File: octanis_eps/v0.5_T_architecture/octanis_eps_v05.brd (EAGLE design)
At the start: 100 x 80 mm, 141 parts, among them IC1 OPA2333DGK, Q3 32.768kHz, Q4 BSS123, U1 BQ24650_RVA_16, U10 CSD16327Q3_DQG_8, U13 CSD16327Q3_DQG_8, U14 CSD16327Q3_DQG_8, U2 TPS630250, U3 TPS630250, U4 TPS630250, U5 TPS2022D, U6 TPS61232, U7 CSD16327Q3_DQG_8, U8 MSP430G2544, U9 CSD16327Q3_DQG_8

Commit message: Arranged parts for EPS v05
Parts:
- moved JP6 220.5 mm to (76.2, 25.4), turned to 90 degrees
- moved JP3 204.9 mm to (11.4, 47.0)
- moved U14 191.1 mm to (72.4, 43.2), turned to 90 degrees
- moved R41 185.6 mm to (2.54, 41.9), turned to 270 degrees
- moved JP1 185.5 mm to (2.54, 47.0), turned to 90 degrees
- moved JP5 185.1 mm to (38.1, 5.08), turned to 90 degrees
- moved R14 184.1 mm to (73.7, 39.4), turned to 270 degrees
- moved R15 180.9 mm to (71.1, 39.4), turned to 90 degrees
- moved JP2 180.1 mm to (15.2, 29.2)
- moved U10 179.8 mm to (67.3, 43.2), turned to 90 degrees
- moved JP4 175.4 mm to (2.54, 6.35), turned to 90 degrees
- moved R10 172.7 mm to (68.6, 39.4), turned to 270 degrees
- moved R11 169.6 mm to (66.0, 39.4), turned to 90 degrees
- moved U13 168.4 mm to (62.2, 43.2), turned to 90 degrees
- moved R34 168.0 mm to (6.35, 5.08), flipped to the bottom, turned to 180 degrees
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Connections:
- removed net N$79: 6.8UH.2, R_SENSE2.I2
- new net N$4: 6.8UH.2, R_SENSE2.I1
- net BAT_OUT: now also JP6.11, JP6.13, JP6.15; no longer JP6.12, JP6.14, JP6.16
- net HEAT1: now also JP6.12; no longer JP6.11
- net HEAT2: now also JP6.14; no longer JP6.13
- net HEAT3: now also JP6.16; no longer JP6.15
- net N$77: now also R_SENSE2.V1; no longer R_SENSE2.V2
- net N$78: now also R_SENSE2.V2; no longer R_SENSE2.V1
- net SC_OUT: now also R_SENSE2.I2; no longer R_SENSE2.I1
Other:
- board size 100 x 80 mm -> 80 x 50 mm

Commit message: started manual routing
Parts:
- moved C15 11.1 mm to (28.1, 44.1), turned to 90 degrees
- moved C16 11.1 mm to (39.8, 42.3), turned to 90 degrees
- moved R116 9.55 mm to (37.1, 33.9), turned to 270 degrees
- moved R118 9.52 mm to (33.9, 32.6), turned to 180 degrees
- moved R103 8.86 mm to (27.6, 36.8), turned to 180 degrees
- moved R17 8.78 mm to (30.1, 44.1), turned to 270 degrees
- moved R13 8.56 mm to (37.7, 42.3), turned to 270 degrees
- moved R107 8.38 mm to (27.6, 39.4), turned to 180 degrees
- moved R119 6.13 mm to (37.7, 38.1), turned to 270 degrees
- moved R117 6.11 mm to (33.9, 34.9), turned to 0 degrees
- moved R104 5.55 mm to (30.1, 36.6), turned to 90 degrees
- moved R108 5.34 mm to (30.1, 40.6), turned to 270 degrees
- moved C18 5.34 mm to (23.9, 26.4), turned to 180 degrees
- moved C2 4.50 mm to (45.0, 30.5)
- moved C_IC1 3.99 mm to (33.9, 41.4), turned to 0 degrees
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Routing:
- net GND: track 0.00 -> 44.1 mm, vias 0 -> 13
- net A_EXT2: track 0.00 -> 23.6 mm
- net N$93: track 0.00 -> 20.3 mm, vias 0 -> 2
- net +3V3: track 0.00 -> 20.1 mm
- net I_IN: track 0.00 -> 17.7 mm, vias 0 -> 2
- net I_OUT: track 0.00 -> 17.5 mm, vias 0 -> 2
- net EN_12V: track 0.00 -> 17.0 mm
- net N$75: track 0.00 -> 16.8 mm
- net EN_5V: track 0.00 -> 15.8 mm
- net EN_3V3_2: track 0.00 -> 14.6 mm
- net EN_3V3_1: track 0.00 -> 13.5 mm
- net A_EXT3: track 0.00 -> 10.7 mm
- net EN_HEAT1: track 0.00 -> 10.4 mm
- net N$23: track 0.00 -> 9.67 mm
- net V_BAT: track 0.00 -> 9.14 mm
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- added copper zone on layer 16, net GND

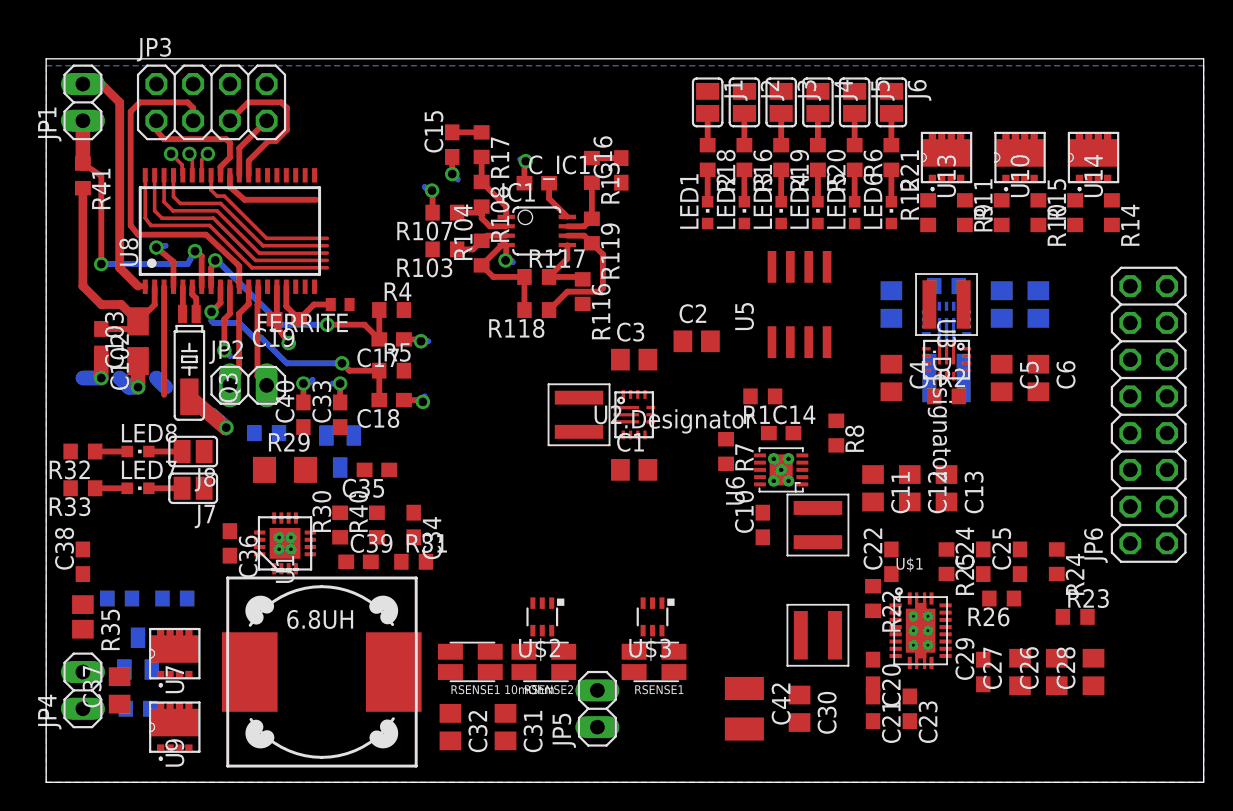
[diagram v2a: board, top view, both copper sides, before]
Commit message: Routed 3.3V, 5V and Solar Cell stepdown
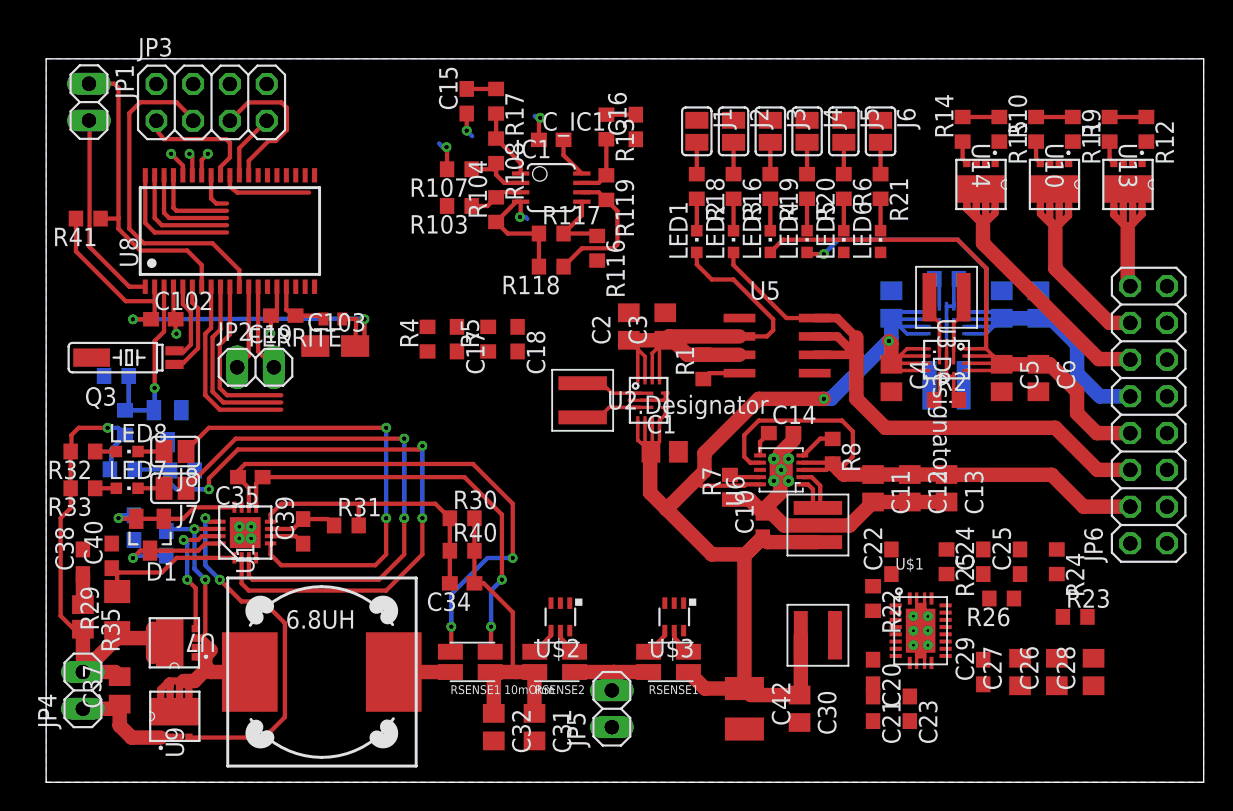
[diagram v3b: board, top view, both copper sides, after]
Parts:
- moved R34 23.0 mm to (4.85, 28.1)
- moved C40 16.5 mm to (4.53, 15.7)
- moved C33 16.2 mm to (6.07, 17.6), flipped to the bottom, turned to 270 degrees
- moved R12 16.1 mm to (76.0, 45.1), turned to 270 degrees
- moved Q4 15.9 mm to (8.40, 24.6), turned to 180 degrees
- moved R29 15.2 mm to (4.91, 11.8), turned to 90 degrees
- moved D1 14.3 mm to (7.18, 17.1), flipped to the top
- moved C103 13.6 mm to (20.0, 30.1), turned to 0 degrees
- moved U13 12.7 mm to (74.8, 41.3), turned to 270 degrees
- moved R39 12.6 mm to (5.45, 24.9), turned to 270 degrees
- moved R14 11.8 mm to (63.3, 45.1), turned to 90 degrees
- moved R9 11.5 mm to (73.5, 45.1), turned to 90 degrees
- moved R27 10.3 mm to (5.26, 21.6), turned to 0 degrees
- moved R28 9.86 mm to (9.42, 21.6), turned to 0 degrees
- moved C18 9.67 mm to (32.6, 30.6), turned to 270 degrees
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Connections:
- net +12V: now also JP6.2; no longer JP6.10
- net +3V3_1: now also JP6.8; no longer JP6.4
- net +3V3_2: now also JP6.10; no longer JP6.6
- net +3V3_M: now also JP6.6; no longer JP6.2
- net +5V: now also JP6.4; no longer JP6.8
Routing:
- net BAT_OUT: track 0.00 -> 100.8 mm, vias 0 -> 2
- net +3V3: track 20.1 -> 75.4 mm, vias 0 -> 2
- net N$64: track 0.00 -> 47.7 mm, vias 0 -> 3
- net +3V3_1: track 0.00 -> 43.1 mm
- net +3V3_M: track 0.00 -> 42.9 mm
- net +5V: track 0.00 -> 40.3 mm
- net +3V3_2: track 0.00 -> 39.5 mm, vias 0 -> 1
- net SC+: track 0.00 -> 38.8 mm, vias 0 -> 1
- net N$71: track 0.00 -> 37.3 mm, vias 0 -> 2
- net N$77: track 0.00 -> 36.2 mm, vias 0 -> 2
- net N$70: track 0.00 -> 32.7 mm, vias 0 -> 2
- net N$78: track 0.00 -> 29.7 mm, vias 0 -> 2
- net GND: track 44.1 -> 73.2 mm, vias 13 -> 6
- net N$76: track 0.00 -> 28.0 mm, vias 0 -> 2
- net N$81: track 0.00 -> 25.2 mm, vias 0 -> 2
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
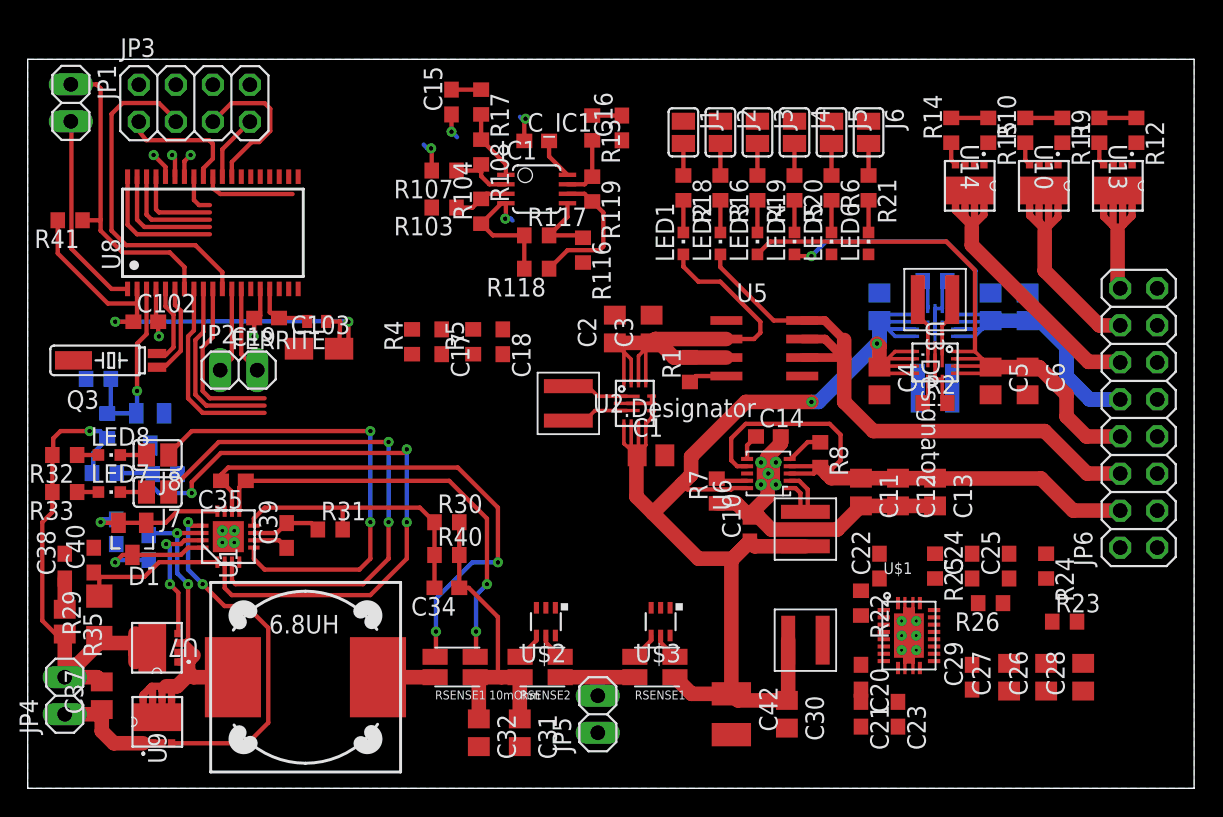
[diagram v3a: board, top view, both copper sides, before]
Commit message: EPS v05 routed, except enable and GND
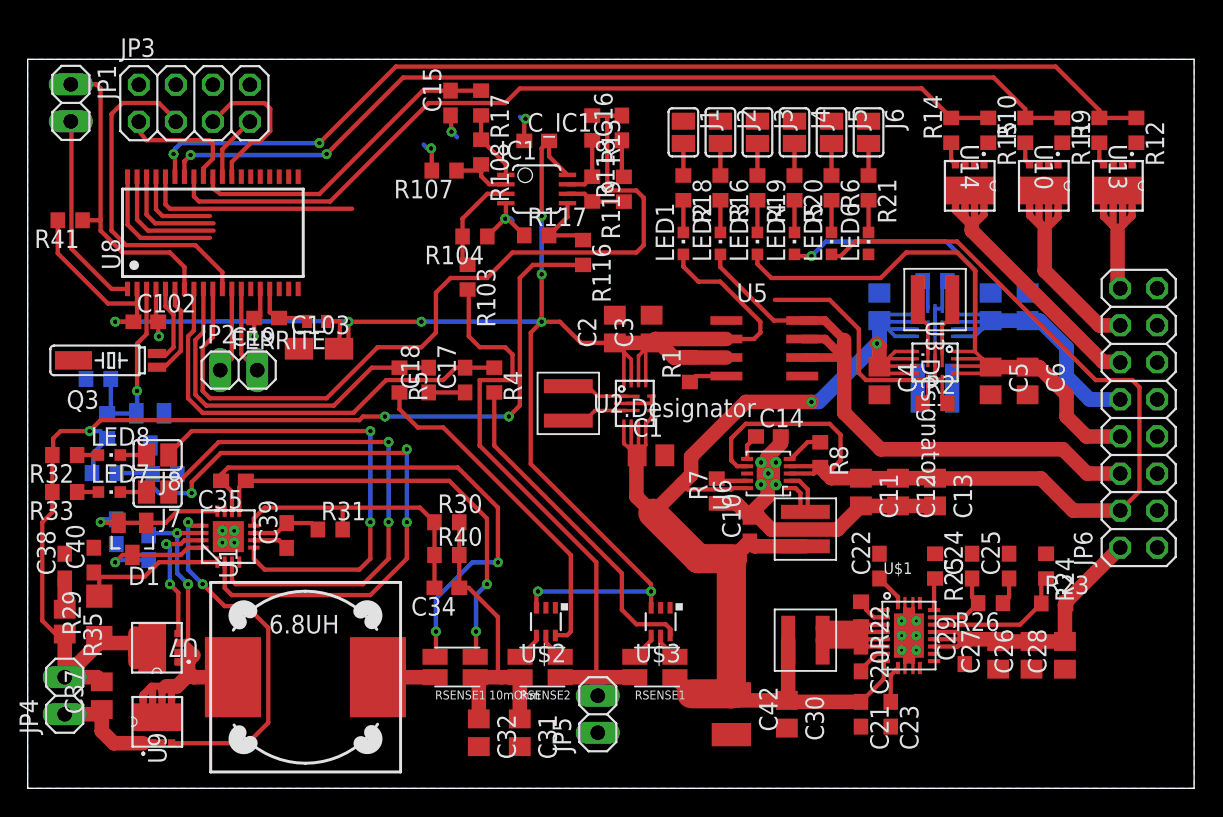
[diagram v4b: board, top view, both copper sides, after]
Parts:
- moved R118 8.09 mm to (40.9, 41.1), turned to 90 degrees
- moved R4 6.22 mm to (32.0, 28.0), turned to 270 degrees
- moved C18 5.72 mm to (27.5, 28.0), turned to 90 degrees
- moved R5 5.69 mm to (25.5, 28.0), turned to 270 degrees
- moved R103 5.04 mm to (30.2, 35.1), turned to 270 degrees
- moved C17 3.08 mm to (30.0, 28.0), turned to 90 degrees
- moved C28 1.95 mm to (71.1, 9.12)
- moved C29 1.82 mm to (64.3, 9.37)
- moved C26 1.80 mm to (68.8, 9.12)
- moved R104 1.78 mm to (30.7, 37.8), turned to 180 degrees
- moved C27 1.68 mm to (66.6, 9.12)
- moved R23 1.46 mm to (70.4, 12.7)
- moved C20 1.25 mm to (57.1, 8.87)
- moved R22 0.75 mm to (57.1, 11.9)
- moved C23 0.50 mm to (59.2, 5.08)
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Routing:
- net EN_HEAT3: track 4.10 -> 72.0 mm, vias 1 -> 2
- net +3V3: track 75.4 -> 139.1 mm, vias 2 -> 8
- net EN_HEAT2: track 4.20 -> 65.1 mm, vias 1 -> 2
- net EN_HEAT1: track 5.38 -> 60.0 mm
- net V_SC: track 13.8 -> 57.6 mm
- net SC+: track 38.8 -> 82.5 mm, vias 1 -> 3
- net BAT+: track 6.45 -> 43.3 mm
- net +5V: track 40.3 -> 75.0 mm
- net N$50: track 0.00 -> 26.0 mm
- net N$26: track 0.00 -> 23.5 mm
- net N$25: track 0.00 -> 22.9 mm
- net +12V: track 0.00 -> 21.7 mm
- net I_OUT: track 13.3 -> 30.4 mm
- net EN_3V3_1: track 7.82 -> 22.5 mm
- net V_BAT: track 8.43 -> 22.3 mm
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
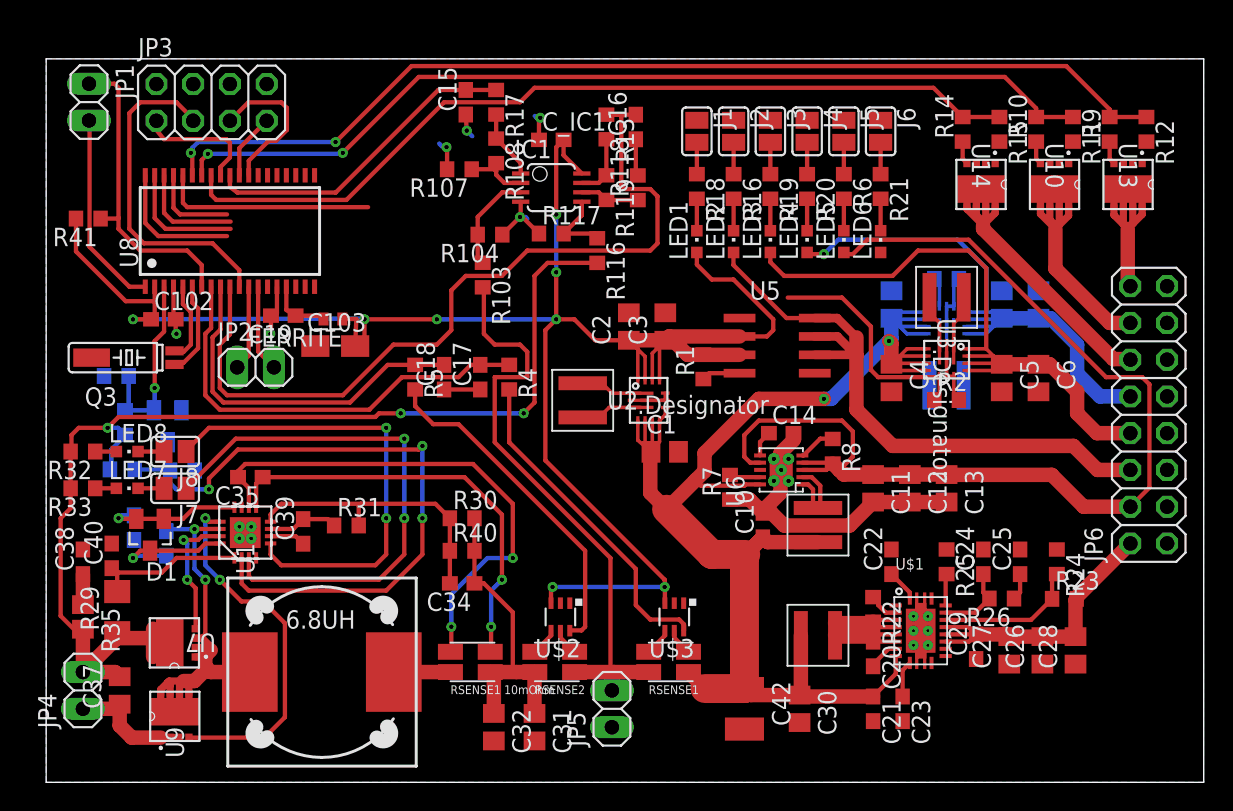
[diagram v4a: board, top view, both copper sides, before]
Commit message: Routed EPS v05, issue with heatpad under Solar and 5V DCDC
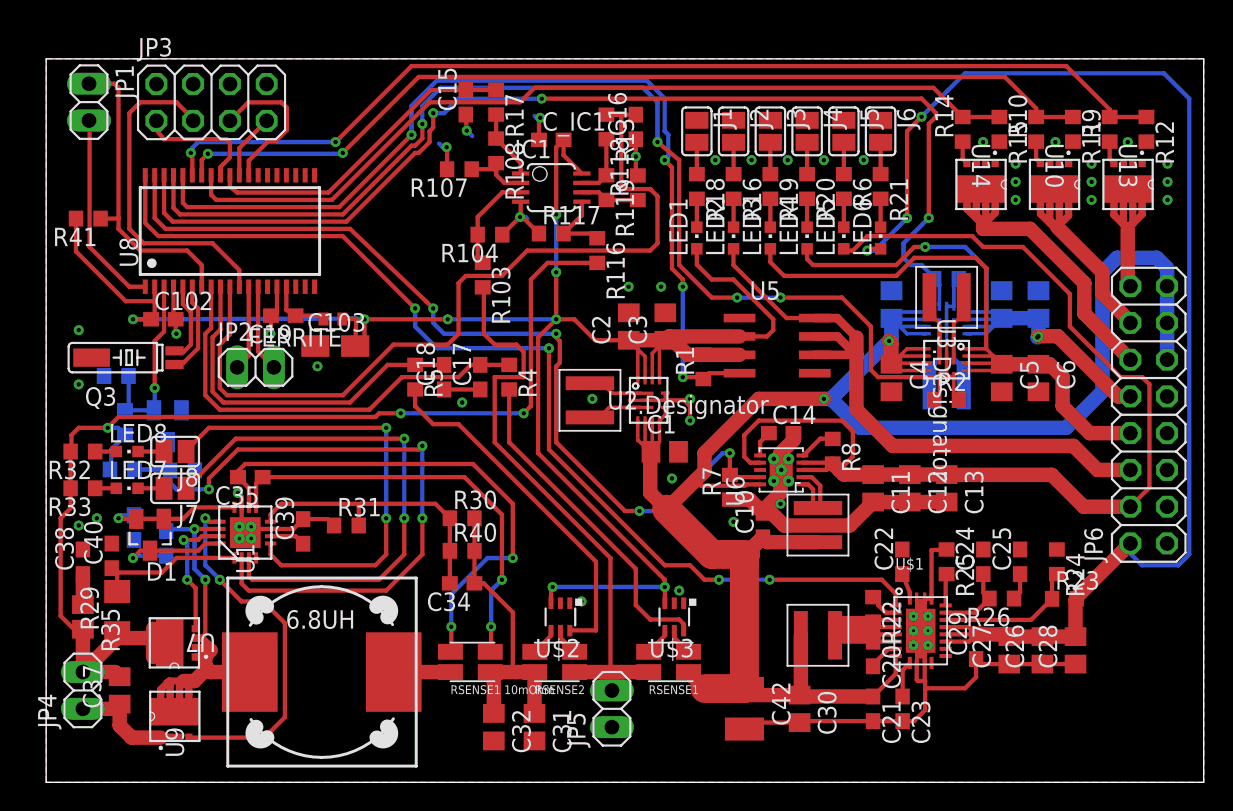
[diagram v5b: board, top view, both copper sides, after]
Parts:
- moved C22 0.75 mm to (59.2, 15.2)
- moved L2 0.50 mm to (37.6, 26.4)
- moved LED1 0.25 mm to (45.0, 37.6)
- moved LED2 0.25 mm to (47.5, 37.6)
- moved LED3 0.25 mm to (50.0, 37.6)
- moved LED4 0.25 mm to (52.6, 37.6)
- moved LED5 0.25 mm to (55.1, 37.6)
- moved LED6 0.25 mm to (57.7, 37.6)
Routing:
- net +12V: track 21.7 -> 91.1 mm, vias 0 -> 3
- net EN_3V3_2: track 9.48 -> 76.9 mm, vias 0 -> 3
- net EN_12V: track 9.32 -> 71.4 mm, vias 0 -> 4
- net EN_3V3_1: track 22.5 -> 78.0 mm, vias 0 -> 4
- net GND: track 73.6 -> 124.6 mm, vias 6 -> 41
- net EN_5V: track 10.7 -> 61.5 mm, vias 0 -> 4
- net EN_3V3_M: track 17.5 -> 64.8 mm, vias 0 -> 4
- net BAT_OUT: track 109.3 -> 149.7 mm
- net N$12: track 0.00 -> 4.11 mm
- net N$11: track 0.00 -> 4.04 mm
- net +5V: track 75.0 -> 76.4 mm
- net HEAT1: track 20.3 -> 21.6 mm
- net N$26: track 23.5 -> 24.7 mm
- net HEAT2: track 16.5 -> 15.7 mm
- net +3V3: track 139.1 -> 139.8 mm
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- added copper zone on layer 1, net GND

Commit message: EPS v05 routing complete
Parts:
- U1: device texasinstruments:RVA16_2P14X2P14 -> octanis_eps_v05:RVA16_2P14X2P14
- U2, U3, U4: value TPS630250 -> Value; device texasinstruments:RNC0014A -> octanis_eps_v05:RNC0014A
- moved C8 0.50 mm to (66.5, 33.0)
- moved C9 0.25 mm to (68.8, 33.0)
- moved JP2 0.14 mm to (14.6, 28.8)
- moved C19 0.11 mm to (16.5, 32.3)
- moved C102 0.10 mm to (8.00, 32.0)
- moved R118 0.09 mm to (40.9, 41.0)
- moved R41 0.09 mm to (3.00, 39.0)
- moved C4 0.06 mm to (58.4, 28.0)
- moved R103 0.06 mm to (30.2, 35.0)
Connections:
- net GND: now also U1.V, U1.V_1, U1.V_2, U1.V_3
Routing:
- net N$8: track 0.00 -> 21.5 mm
- net +3V3_2: track 39.9 -> 42.2 mm, vias 3 -> 2
- net EN_3V3_2: track 76.9 -> 75.1 mm
- net A_EXT1: track 8.64 -> 7.73 mm
- net GND: track 124.6 -> 124.1 mm, vias 41 -> 63
